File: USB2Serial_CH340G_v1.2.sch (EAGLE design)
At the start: 22 parts, among them CN1 UART, CN2 47346-0001, IC1 AMS1117-3.3, U2 FT232RL

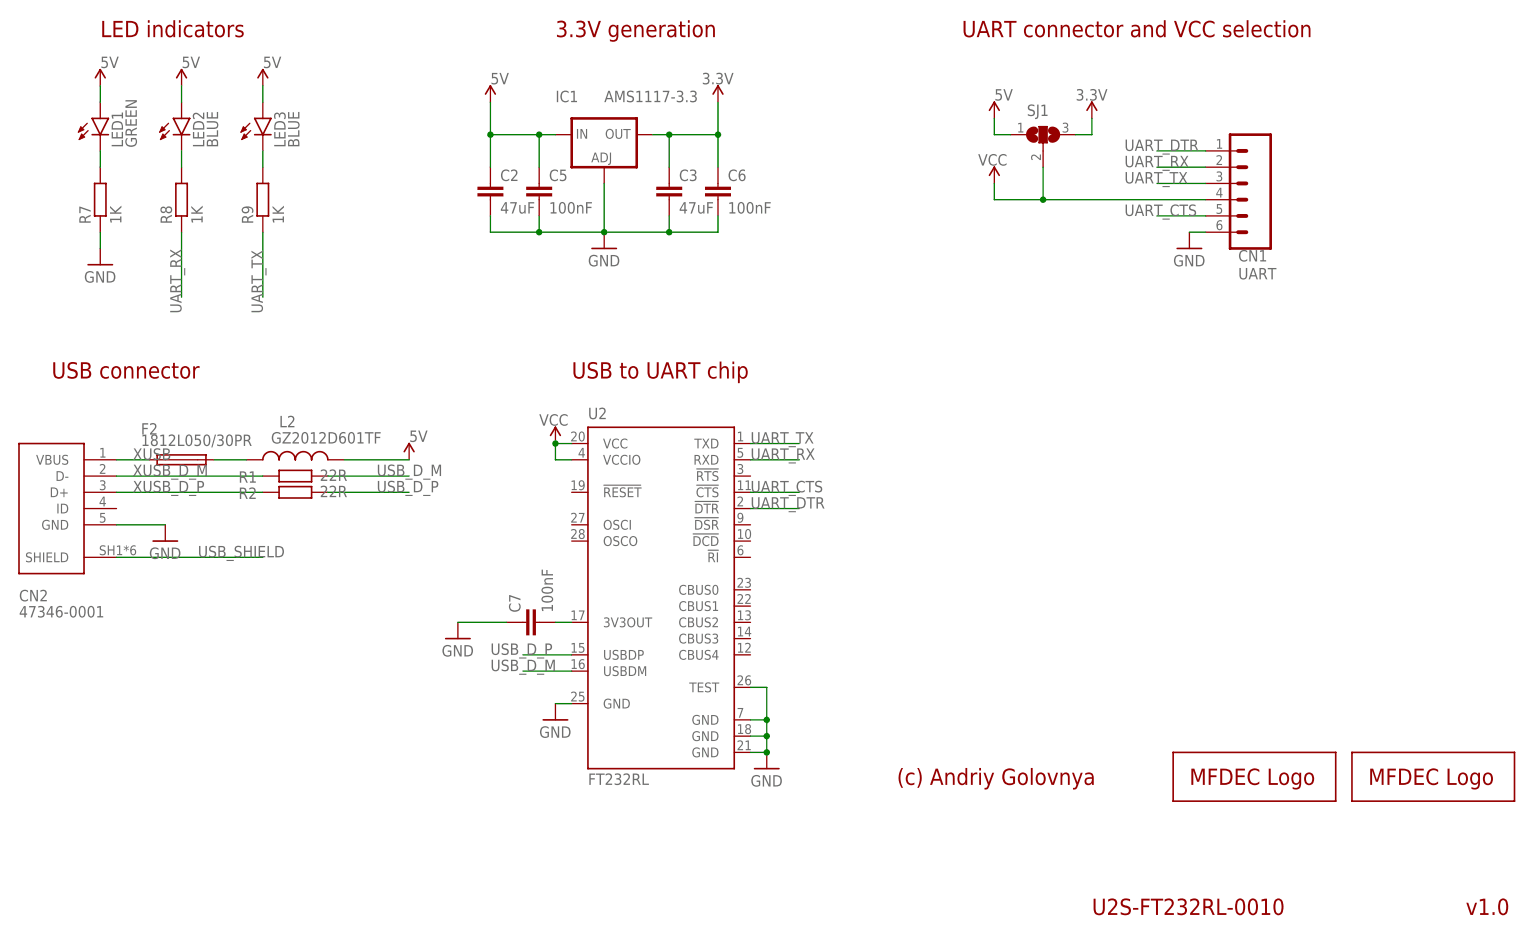
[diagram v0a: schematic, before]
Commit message: Added C2. Added 1.2 for CH240G board.
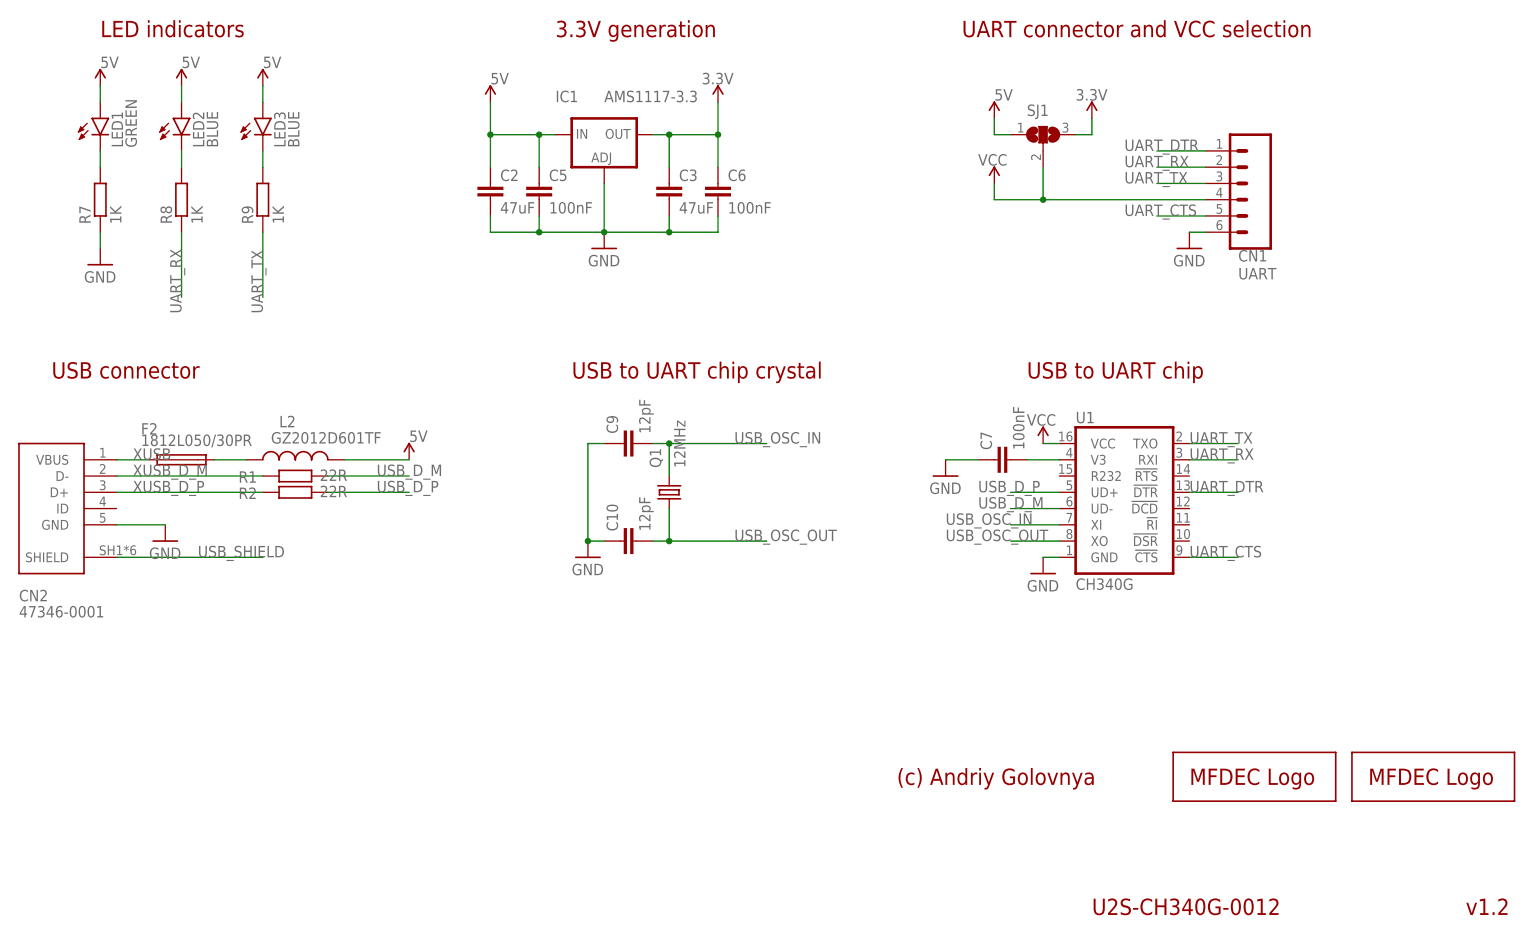
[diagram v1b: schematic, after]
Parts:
- removed U2: FT232RL, ftdichip:FT232RL
- added C10, C9: 12pF, rcl:C-EUC0402
- added Q1: 12MHz, crystal-geyer_V1_0:KX-7
- added U1: CH340G, SparkFun-IC-Comms:CH340GSMD
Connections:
- new net USB_OSC_IN: C9.2, Q1.2, U1.XI
- new net USB_OSC_OUT: C10.2, Q1.1, U1.XO
- net GND: now also C10.1, C9.1, U1.GND; no longer U2.GND, U2.GND@1, U2.GND@2, U2.GND@A, U2.TEST
- net N$6: now also U1.V3; no longer U2.3V3OUT
- net UART_CTS: now also U1.!CTS; no longer U2.!CTS
- net UART_DTR: now also U1.!DTR; no longer U2.!DTR
- net UART_RX: now also U1.RXI; no longer U2.RXD
- net UART_TX: now also U1.TXO; no longer U2.TXD
- net USB_D_M: now also U1.UD-; no longer U2.USBDM
- net USB_D_P: now also U1.UD+; no longer U2.USBDP
- net VCC: now also U1.VCC; no longer U2.VCC, U2.VCCIO
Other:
- note added: "U2S-CH340G-0012"
- note added: "USB to UART chip crystal"
- note added: "v1.2"
- note removed: "U2S-FT232RL-0010"
- note removed: "v1.0"
- moved on the sheet: C7
